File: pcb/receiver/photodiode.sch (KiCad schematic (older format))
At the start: 110 parts, among them Q201 BFR31,215, Q202 MMBT2222A-7-F, Q203 MMBT2222A-7-F, Q204 MMBT2222A-7-F, Q205 MMBT2222A-7-F, Q206 MMBT2222A-7-F, Q207 TF414T5G, U201 ADR550ARTZ-REEL7, U202 TL974IPWR, U203 MAX4477AUA+, U204 OPA2141AIDR, U205 NLAS4599DFT2G

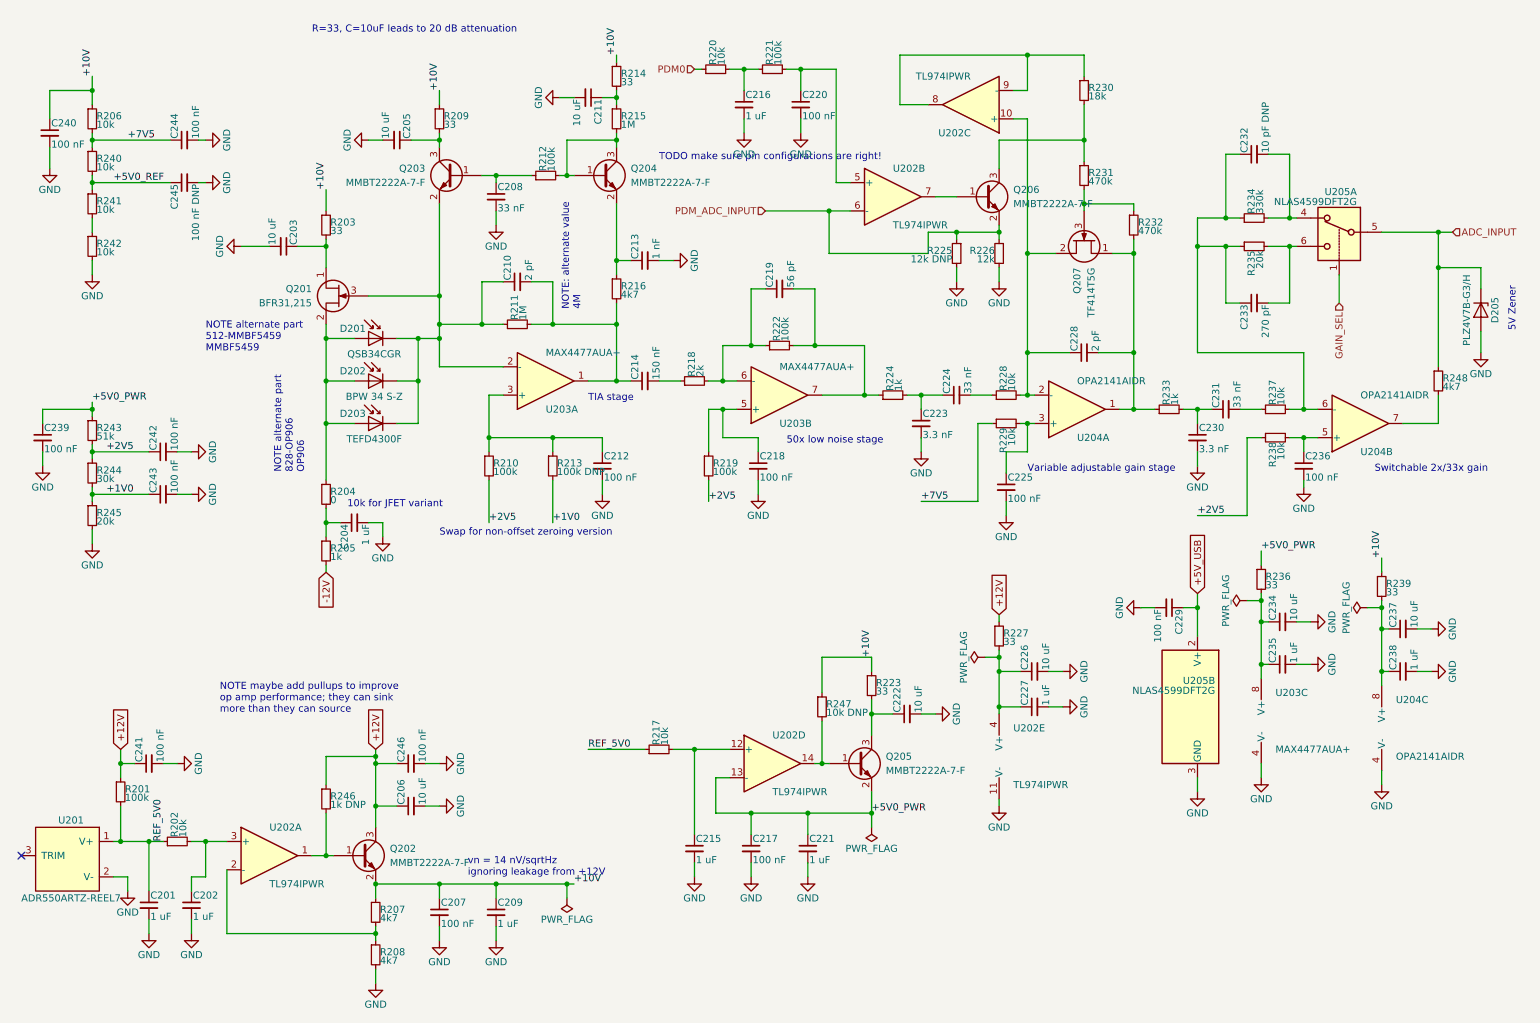
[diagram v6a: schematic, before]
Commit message: Add copper fills and outline, autofill test point footprints, TODO finish placing test points and moving silkscreen
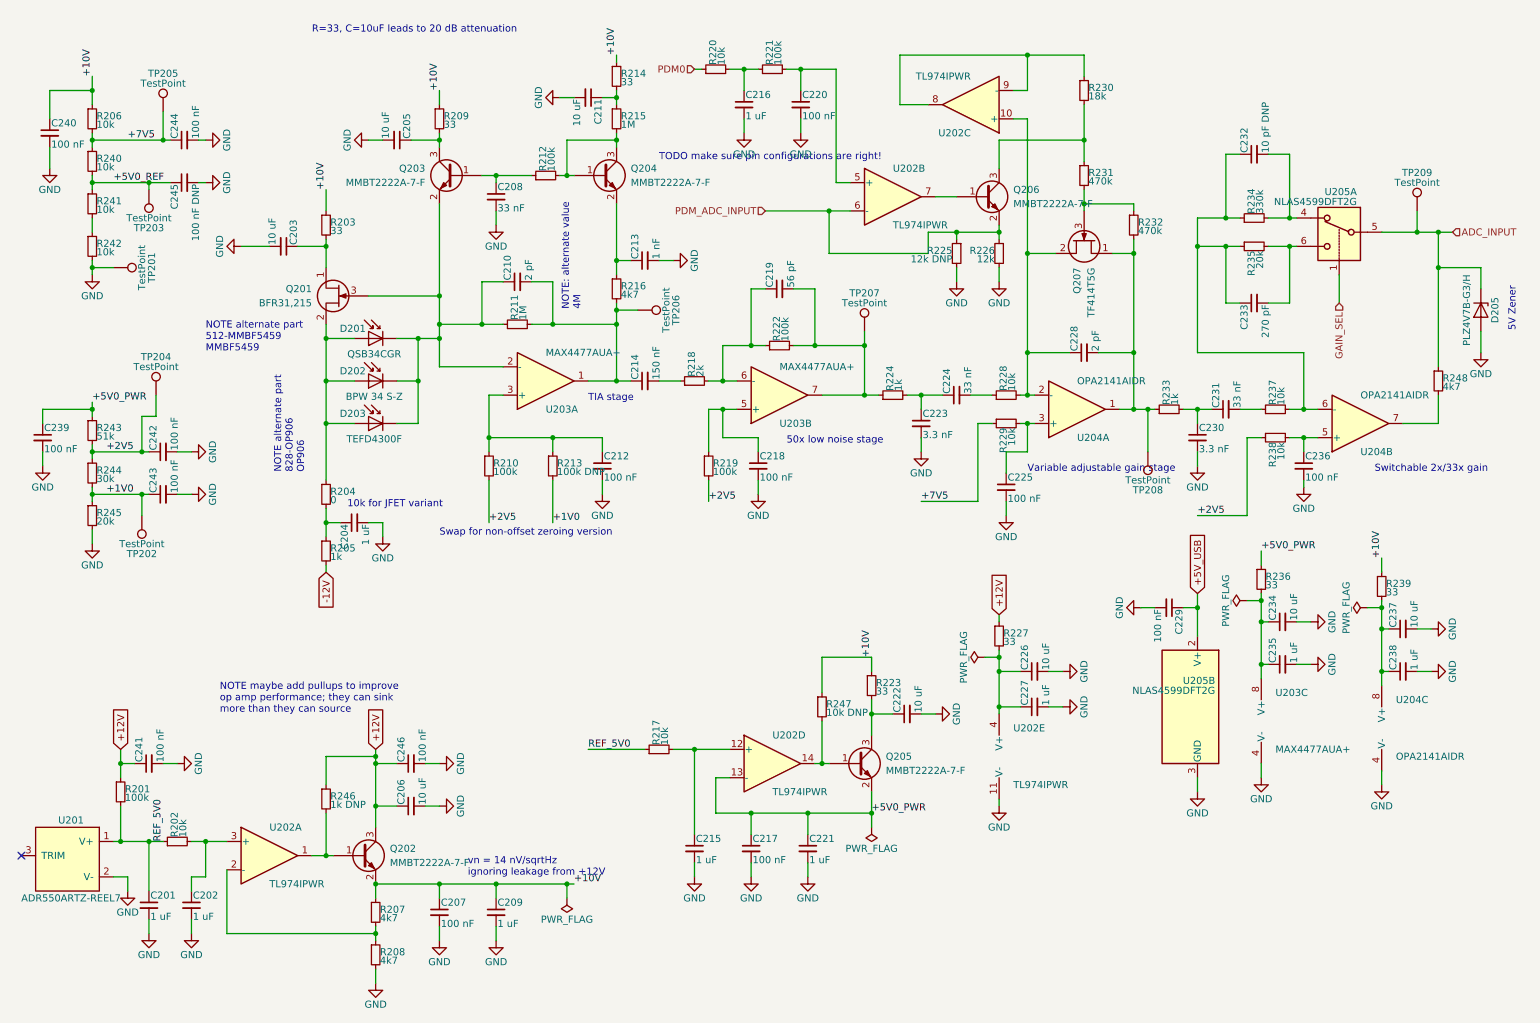
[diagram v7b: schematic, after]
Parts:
- added TP201, TP202, TP203, TP204, TP205, TP206, TP207, TP208, TP209: TestPoint, Measurement_Points:Measurement_Point_Round-SMD-Pad_Small, symbol Connector:TestPoint
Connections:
- net +1V0: now also TP202.1
- net +2V5: now also TP204.1
- net +5V0_REF: now also TP203.1
- net +7V5: now also TP205.1
- net ADC_INPUT: now also TP209.1
- net GND: now also TP201.1
- net at C210.2, C214.1, R211.2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: now also TP206.1
- net at C219.2, R222.2, R224.1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: now also TP207.1
- net at C228.2, Q207.1 (S), R232.2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: now also TP208.1
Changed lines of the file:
@@
 Connection ~ 4800 2800
 Wire Wire Line
-	4800 2800 4800 2650
+	4800 2800 4800 2700
 Wire Wire Line
 	4800 1950 4800 2350
@@
 	8900 3400 9000 3400
 Wire Wire Line
-	8450 3400 8600 3400
+	8450 3400 8550 3400
 Connection ~ 8450 3400
 $Comp
@@
 $EndComp
 Wire Wire Line
-	1100 2350 1100 2450
+	1100 2350 1100 2400
 Wire Wire Line
 	1100 2050 1100 2150
@@
 	1700 4000 1800 4000
 Wire Wire Line
-	1500 3700 1100 3700
+	1500 3700 1450 3700
 Connection ~ 1100 3700
 Wire Wire Line
@@
 	1100 1450 1100 1500
 Wire Wire Line
-	1100 1500 1650 1500
-Wire Wire Line
-	1100 1800 1650 1800
-Wire Wire Line
-	1100 4000 1500 4000
+	1100 1500 1600 1500
+Wire Wire Line
+	1100 1800 1500 1800
+Wire Wire Line
+	1100 4000 1450 4000
 Text GLabel 1300 5800 1    50   Input ~ 0
 +12V
@@
 +2V5
 Wire Wire Line
-	10200 2150 10600 2150
+	10200 2150 10450 2150
 $Comp
 L Device:R_Small R248
@@
 Wire Wire Line
 	2750 3500 2750 3900
+$Comp
+L Connector:TestPoint TP207
+U 1 1 5C2FEC78
+P 6550 2850
+F 0 "TP207" H 6550 3120 50  0000 C CNN
+F 1 "TestPoint" H 6550 3050 50  0000 C CNN
+F 2 "Measurement_Points:Measurement_Point_Round-SMD-Pad_Small" H 6750 2850 50  0001 C CNN
+F 3 "~" H 6750 2850 50  0001 C CNN
+F 4 "NoPart" H 6750 2850 50  0001 C CNN "Mouser"
+	1    6550 2850
+	1    0    0    -1
+$EndComp
+Wire Wire Line
+	6550 2850 6550 2950
+Connection ~ 6550 2950
+$Comp
+L Connector:TestPoint TP208
+U 1 1 5C32152F
+P 8550 3700
+F 0 "TP208" H 8550 3970 50  0000 C CNN
+F 1 "TestPoint" H 8550 3900 50  0000 C CNN
+F 2 "Measurement_Points:Measurement_Point_Round-SMD-Pad_Small" H 8750 3700 50  0001 C CNN
+F 3 "~" H 8750 3700 50  0001 C CNN
+F 4 "NoPart" H 8750 3700 50  0001 C CNN "Mouser"
+	1    8550 3700
+	-1   0    0    1
+$EndComp
+Wire Wire Line
+	8550 3700 8550 3400
+Connection ~ 8550 3400
+Wire Wire Line
+	8550 3400 8600 3400
+$Comp
+L Connector:TestPoint TP209
+U 1 1 5C34427D
+P 10450 2000
+F 0 "TP209" H 10450 2270 50  0000 C CNN
+F 1 "TestPoint" H 10450 2200 50  0000 C CNN
+F 2 "Measurement_Points:Measurement_Point_Round-SMD-Pad_Small" H 10650 2000 50  0001 C CNN
+F 3 "~" H 10650 2000 50  0001 C CNN
+F 4 "NoPart" H 10650 2000 50  0001 C CNN "Mouser"
+	1    10450 2000
+	1    0    0    -1
+$EndComp
+Wire Wire Line
+	10450 2000 10450 2150
+Connection ~ 10450 2150
+Wire Wire Line
+	10450 2150 10600 2150
+$Comp
+L Connector:TestPoint TP201
+U 1 1 5C3675CA
+P 1250 2400
+F 0 "TP201" H 1250 2670 50  0000 C CNN
+F 1 "TestPoint" H 1250 2600 50  0000 C CNN
+F 2 "Measurement_Points:Measurement_Point_Round-SMD-Pad_Small" H 1450 2400 50  0001 C CNN
+F 3 "~" H 1450 2400 50  0001 C CNN
+F 4 "NoPart" H 1450 2400 50  0001 C CNN "Mouser"
+	1    1250 2400
+	0    1    1    0
+$EndComp
+Wire Wire Line
+	1250 2400 1100 2400
+Connection ~ 1100 2400
+Wire Wire Line
+	1100 2400 1100 2450
+$Comp
+L Connector:TestPoint TP203
+U 1 1 5C38B0A8
+P 1500 1850
+F 0 "TP203" H 1500 2120 50  0000 C CNN
+F 1 "TestPoint" H 1500 2050 50  0000 C CNN
+F 2 "Measurement_Points:Measurement_Point_Round-SMD-Pad_Small" H 1700 1850 50  0001 C CNN
+F 3 "~" H 1700 1850 50  0001 C CNN
+F 4 "NoPart" H 1700 1850 50  0001 C CNN "Mouser"
+	1    1500 1850
+	-1   0    0    1
+$EndComp
+Wire Wire Line
+	1500 1850 1500 1800
+Connection ~ 1500 1800
+Wire Wire Line
+	1500 1800 1650 1800
+$Comp
+L Connector:TestPoint TP205
+U 1 1 5C3AF0B6
+P 1600 1300
+F 0 "TP205" H 1600 1570 50  0000 C CNN
+F 1 "TestPoint" H 1600 1500 50  0000 C CNN
+F 2 "Measurement_Points:Measurement_Point_Round-SMD-Pad_Small" H 1800 1300 50  0001 C CNN
+F 3 "~" H 1800 1300 50  0001 C CNN
+F 4 "NoPart" H 1800 1300 50  0001 C CNN "Mouser"
+	1    1600 1300
+	1    0    0    -1
+$EndComp
+Wire Wire Line
+	1600 1300 1600 1500
+Connection ~ 1600 1500
+Wire Wire Line
+	1600 1500 1650 1500
+$Comp
+L Connector:TestPoint TP204
+U 1 1 5C3D37D0
+P 1550 3300
+F 0 "TP204" H 1550 3570 50  0000 C CNN
+F 1 "TestPoint" H 1550 3500 50  0000 C CNN
+F 2 "Measurement_Points:Measurement_Point_Round-SMD-Pad_Small" H 1750 3300 50  0001 C CNN
+F 3 "~" H 1750 3300 50  0001 C CNN
+F 4 "NoPart" H 1750 3300 50  0001 C CNN "Mouser"
+	1    1550 3300
+	1    0    0    -1
+$EndComp
+Wire Wire Line
+	1550 3300 1550 3450
+Wire Wire Line
+	1550 3450 1450 3450
+Wire Wire Line
+	1450 3450 1450 3700
+Connection ~ 1450 3700
+Wire Wire Line
+	1450 3700 1100 3700
+$Comp
+L Connector:TestPoint TP202
+U 1 1 5C3F933E
+P 1450 4150
+F 0 "TP202" H 1450 4420 50  0000 C CNN
+F 1 "TestPoint" H 1450 4350 50  0000 C CNN
+F 2 "Measurement_Points:Measurement_Point_Round-SMD-Pad_Small" H 1650 4150 50  0001 C CNN
+F 3 "~" H 1650 4150 50  0001 C CNN
+F 4 "NoPart" H 1650 4150 50  0001 C CNN "Mouser"
+	1    1450 4150
+	-1   0    0    1
+$EndComp
+Wire Wire Line
+	1450 4150 1450 4000
+Connection ~ 1450 4000
+Wire Wire Line
+	1450 4000 1500 4000
+$Comp
+L Connector:TestPoint TP206
+U 1 1 5C4200FC
+P 4950 2700
+F 0 "TP206" H 4950 2970 50  0000 C CNN
+F 1 "TestPoint" H 4950 2900 50  0000 C CNN
+F 2 "Measurement_Points:Measurement_Point_Round-SMD-Pad_Small" H 5150 2700 50  0001 C CNN
+F 3 "~" H 5150 2700 50  0001 C CNN
+F 4 "NoPart" H 5150 2700 50  0001 C CNN "Mouser"
+	1    4950 2700
+	0    1    1    0
+$EndComp
+Wire Wire Line
+	4950 2700 4800 2700
+Connection ~ 4800 2700
+Wire Wire Line
+	4800 2700 4800 2650
 $EndSCHEMATC

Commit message: Finish silkscreen stuff
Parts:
- removed TP203: TestPoint, Measurement_Points:Measurement_Point_Round-SMD-Pad_Small, symbol Connector:TestPoint
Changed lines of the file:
@@
 	1100 1500 1600 1500
-Wire Wire Line
-	1100 1800 1500 1800
 Wire Wire Line
 	1100 4000 1450 4000
@@
 	1100 2400 1100 2450
 $Comp
-L Connector:TestPoint TP203
-U 1 1 5C38B0A8
-P 1500 1850
-F 0 "TP203" H 1500 2120 50  0000 C CNN
-F 1 "TestPoint" H 1500 2050 50  0000 C CNN
-F 2 "Measurement_Points:Measurement_Point_Round-SMD-Pad_Small" H 1700 1850 50  0001 C CNN
-F 3 "~" H 1700 1850 50  0001 C CNN
-F 4 "NoPart" H 1700 1850 50  0001 C CNN "Mouser"
-	1    1500 1850
-	-1   0    0    1
-$EndComp
-Wire Wire Line
-	1500 1850 1500 1800
-Connection ~ 1500 1800
-Wire Wire Line
-	1500 1800 1650 1800
-$Comp
 L Connector:TestPoint TP205
 U 1 1 5C3AF0B6
@@
 Wire Wire Line
 	4800 2700 4800 2650
+Wire Wire Line
+	1100 1800 1650 1800
 $EndSCHEMATC
